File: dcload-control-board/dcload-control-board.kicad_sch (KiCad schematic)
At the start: 6 parts, among them J100 Conn_01x08_Female, J101 Conn_01x08_Female, J102 Conn_01x03_Male, J103 Conn_01x03_Male

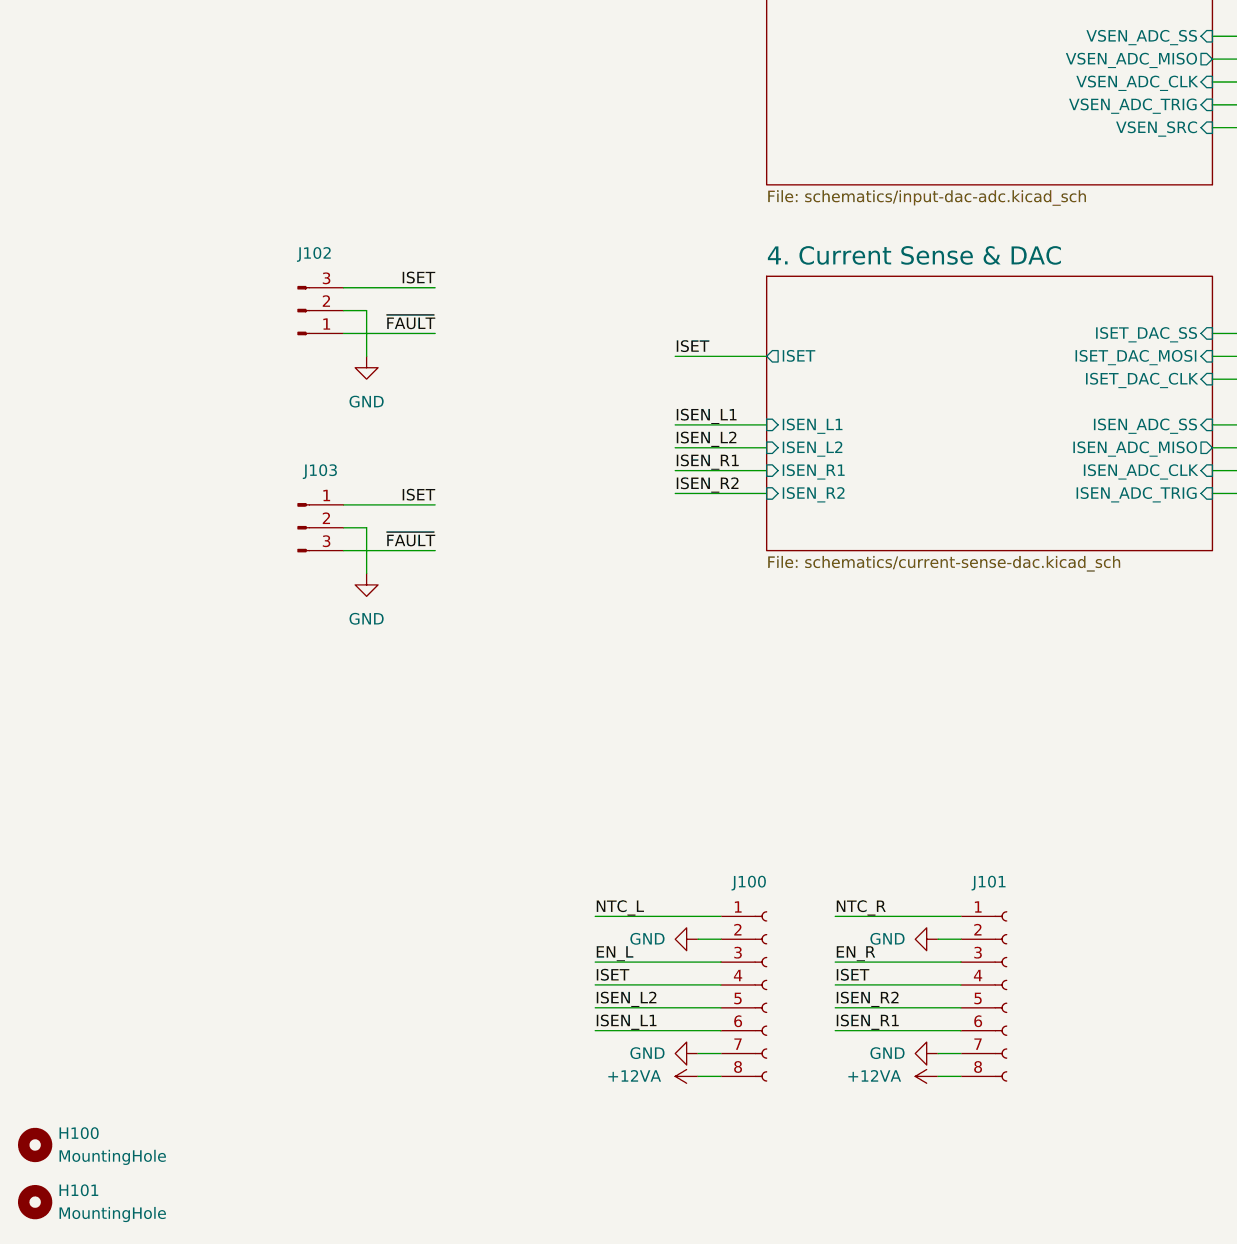
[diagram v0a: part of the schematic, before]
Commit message: add: interface panel board
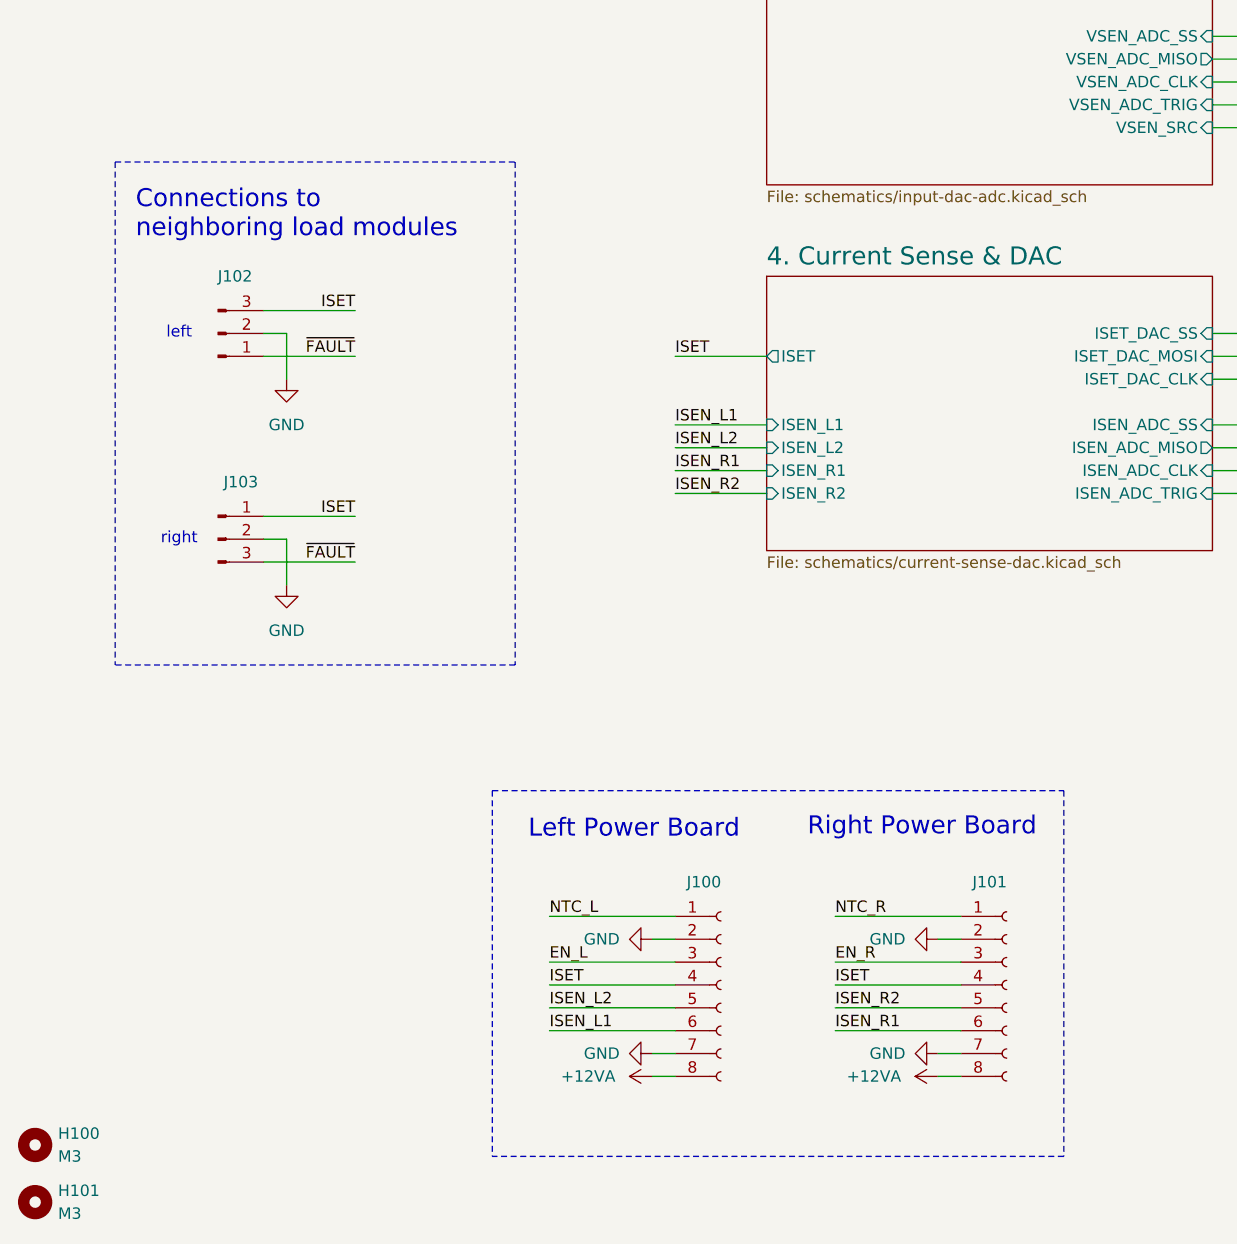
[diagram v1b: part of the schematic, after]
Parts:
- H100, H101: value MountingHole -> M3
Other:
- note added: "Connections to neighboring load modules"
- note added: "Left Power Board"
- note added: "Right Power Board"
- note added: "left"
- note added: "right"
- moved on the sheet: J100, J102, J103
